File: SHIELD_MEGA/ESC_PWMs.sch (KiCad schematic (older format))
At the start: 4 parts

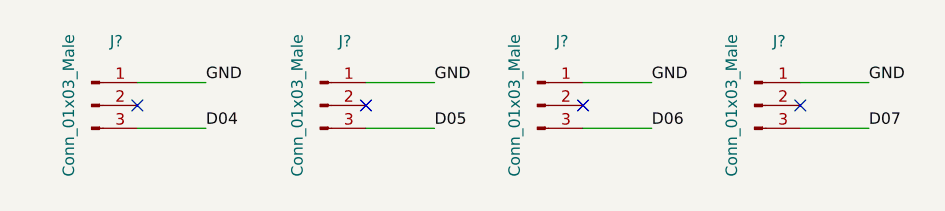
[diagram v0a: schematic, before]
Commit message: Updating labels to hierarch in digital pins sheet
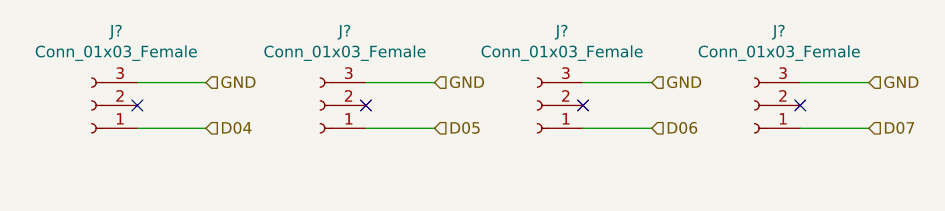
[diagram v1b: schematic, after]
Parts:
- removed J? (x4): Conn_01x03_Male, symbol Connector:Conn_01x03_Male
- added J? (x4): Conn_01x03_Female, symbol Connector:Conn_01x03_Female
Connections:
- net D04: now also J?.1 (Pin_1)
- net D05: now also J?.1 (Pin_1)
- net D06: now also J?.1 (Pin_1)
- net D07: now also J?.1 (Pin_1)
- net GND: now also J?.3 (Pin_3), J?.3 (Pin_3), J?.3 (Pin_3), J?.3 (Pin_3)
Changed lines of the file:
@@
 $Descr A4 11693 8268
 encoding utf-8
-Sheet 4 9
+Sheet 3 10
 Title ""
 Date ""
@@
 Comment4 ""
 $EndDescr
-$Comp
-L Connector:Conn_01x03_Male J?
-U 1 1 61965A08
-P 4250 3900
-F 0 "J?" H 4358 4181 50  0000 C CNN
-F 1 "Conn_01x03_Male" V 4150 3900 50  0000 C CNN
-F 2 "" H 4250 3900 50  0001 C CNN
-F 3 "~" H 4250 3900 50  0001 C CNN
-	1    4250 3900
-	1    0    0    -1
-$EndComp
-$Comp
-L Connector:Conn_01x03_Male J?
-U 1 1 619660C7
-P 5250 3900
-F 0 "J?" H 5358 4181 50  0000 C CNN
-F 1 "Conn_01x03_Male" V 5150 3900 50  0000 C CNN
-F 2 "" H 5250 3900 50  0001 C CNN
-F 3 "~" H 5250 3900 50  0001 C CNN
-	1    5250 3900
-	1    0    0    -1
-$EndComp
-$Comp
-L Connector:Conn_01x03_Male J?
-U 1 1 619668B2
-P 6200 3900
-F 0 "J?" H 6308 4181 50  0000 C CNN
-F 1 "Conn_01x03_Male" V 6100 3900 50  0000 C CNN
-F 2 "" H 6200 3900 50  0001 C CNN
-F 3 "~" H 6200 3900 50  0001 C CNN
-	1    6200 3900
-	1    0    0    -1
-$EndComp
-$Comp
-L Connector:Conn_01x03_Male J?
-U 1 1 619670CA
-P 7150 3900
-F 0 "J?" H 7258 4181 50  0000 C CNN
-F 1 "Conn_01x03_Male" V 7050 3900 50  0000 C CNN
-F 2 "" H 7150 3900 50  0001 C CNN
-F 3 "~" H 7150 3900 50  0001 C CNN
-	1    7150 3900
-	1    0    0    -1
-$EndComp
 NoConn ~ 4450 3900
 NoConn ~ 5450 3900
 NoConn ~ 6400 3900
 NoConn ~ 7350 3900
-Text Label 4750 3800 0    50   ~ 0
-GND
 Wire Wire Line
 	4750 3800 4450 3800
-Text Label 4750 4000 0    50   ~ 0
-D04
 Wire Wire Line
 	4750 4000 4450 4000
 Wire Wire Line
 	5450 3800 5750 3800
-Text Label 5750 3800 0    50   ~ 0
-GND
-Text Label 5750 4000 0    50   ~ 0
-D05
 Wire Wire Line
 	5750 4000 5450 4000
 Wire Wire Line
 	6400 3800 6700 3800
-Text Label 6700 3800 0    50   ~ 0
-GND
-Text Label 6700 4000 0    50   ~ 0
-D06
 Wire Wire Line
 	6700 4000 6400 4000
 Wire Wire Line
 	7350 3800 7650 3800
-Text Label 7650 3800 0    50   ~ 0
-GND
-Text Label 7650 4000 0    50   ~ 0
-D07
 Wire Wire Line
 	7650 4000 7350 4000
+Text HLabel 4750 4000 2    50   Input ~ 0
+D04
+Text HLabel 5750 4000 2    50   Input ~ 0
+D05
+Text HLabel 6700 4000 2    50   Input ~ 0
+D06
+Text HLabel 7650 4000 2    50   Input ~ 0
+D07
+Text HLabel 4750 3800 2    50   Input ~ 0
+GND
+Text HLabel 5750 3800 2    50   Input ~ 0
+GND
+Text HLabel 6700 3800 2    50   Input ~ 0
+GND
+Text HLabel 7650 3800 2    50   Input ~ 0
+GND
+$Comp
+L Connector:Conn_01x03_Female J?
+U 1 1 61B84D65
+P 4250 3900
+F 0 "J?" H 4142 3575 50  0000 C CNN
+F 1 "Conn_01x03_Female" H 4142 3666 50  0000 C CNN
+F 2 "" H 4250 3900 50  0001 C CNN
+F 3 "~" H 4250 3900 50  0001 C CNN
+	1    4250 3900
+	-1   0    0    1
+$EndComp
+$Comp
+L Connector:Conn_01x03_Female J?
+U 1 1 61B866DB
+P 5250 3900
+F 0 "J?" H 5142 3575 50  0000 C CNN
+F 1 "Conn_01x03_Female" H 5142 3666 50  0000 C CNN
+F 2 "" H 5250 3900 50  0001 C CNN
+F 3 "~" H 5250 3900 50  0001 C CNN
+	1    5250 3900
+	-1   0    0    1
+$EndComp
+$Comp
+L Connector:Conn_01x03_Female J?
+U 1 1 61B88889
+P 6200 3900
+F 0 "J?" H 6092 3575 50  0000 C CNN
+F 1 "Conn_01x03_Female" H 6092 3666 50  0000 C CNN
+F 2 "" H 6200 3900 50  0001 C CNN
+F 3 "~" H 6200 3900 50  0001 C CNN
+	1    6200 3900
+	-1   0    0    1
+$EndComp
+$Comp
+L Connector:Conn_01x03_Female J?
+U 1 1 61B8957B
+P 7150 3900
+F 0 "J?" H 7042 3575 50  0000 C CNN
+F 1 "Conn_01x03_Female" H 7042 3666 50  0000 C CNN
+F 2 "" H 7150 3900 50  0001 C CNN
+F 3 "~" H 7150 3900 50  0001 C CNN
+	1    7150 3900
+	-1   0    0    1
+$EndComp
 $EndSCHEMATC

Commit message: Anotations of ref. parts in pwm esc's sheet
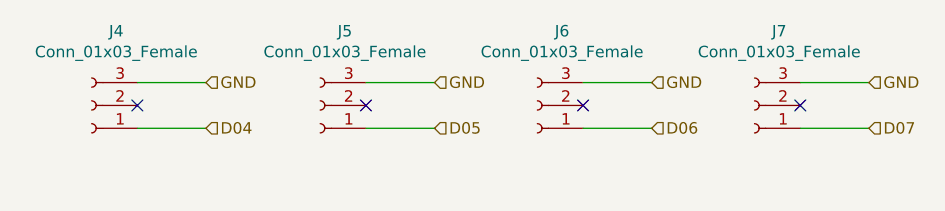
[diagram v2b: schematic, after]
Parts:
- gave numbers to parts that had none: 4
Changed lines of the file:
@@
 encoding utf-8
 Sheet 3 10
-Title ""
-Date ""
-Rev ""
-Comp ""
+Title "SHIELD ARDUINO MEGA"
+Date "2021-11-21"
+Rev "V1"
+Comp "PROEX - UNIFEI"
 Comment1 ""
 Comment2 ""
 Comment3 ""
-Comment4 ""
+Comment4 "LINCOLN WALLACE VELOSO ALMEIDA"
 $EndDescr
 NoConn ~ 4450 3900
@@
 GND
 $Comp
-L Connector:Conn_01x03_Female J?
+L Connector:Conn_01x03_Female J4
 U 1 1 61B84D65
 P 4250 3900
-F 0 "J?" H 4142 3575 50  0000 C CNN
+F 0 "J4" H 4142 3575 50  0000 C CNN
 F 1 "Conn_01x03_Female" H 4142 3666 50  0000 C CNN
 F 2 "" H 4250 3900 50  0001 C CNN
@@
 $EndComp
 $Comp
-L Connector:Conn_01x03_Female J?
+L Connector:Conn_01x03_Female J5
 U 1 1 61B866DB
 P 5250 3900
-F 0 "J?" H 5142 3575 50  0000 C CNN
+F 0 "J5" H 5142 3575 50  0000 C CNN
 F 1 "Conn_01x03_Female" H 5142 3666 50  0000 C CNN
 F 2 "" H 5250 3900 50  0001 C CNN
@@
 $EndComp
 $Comp
-L Connector:Conn_01x03_Female J?
+L Connector:Conn_01x03_Female J6
 U 1 1 61B88889
 P 6200 3900
-F 0 "J?" H 6092 3575 50  0000 C CNN
+F 0 "J6" H 6092 3575 50  0000 C CNN
 F 1 "Conn_01x03_Female" H 6092 3666 50  0000 C CNN
 F 2 "" H 6200 3900 50  0001 C CNN
@@
 $EndComp
 $Comp
-L Connector:Conn_01x03_Female J?
+L Connector:Conn_01x03_Female J7
 U 1 1 61B8957B
 P 7150 3900
-F 0 "J?" H 7042 3575 50  0000 C CNN
+F 0 "J7" H 7042 3575 50  0000 C CNN
 F 1 "Conn_01x03_Female" H 7042 3666 50  0000 C CNN
 F 2 "" H 7150 3900 50  0001 C CNN
